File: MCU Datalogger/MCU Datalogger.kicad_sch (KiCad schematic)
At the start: 25 parts, among them U1 24LC1025, U2 DS1337S_, U3 24LC1025, U4 ATMEGA328P-AU, Y1 32.768KHz, Y2 16MHz

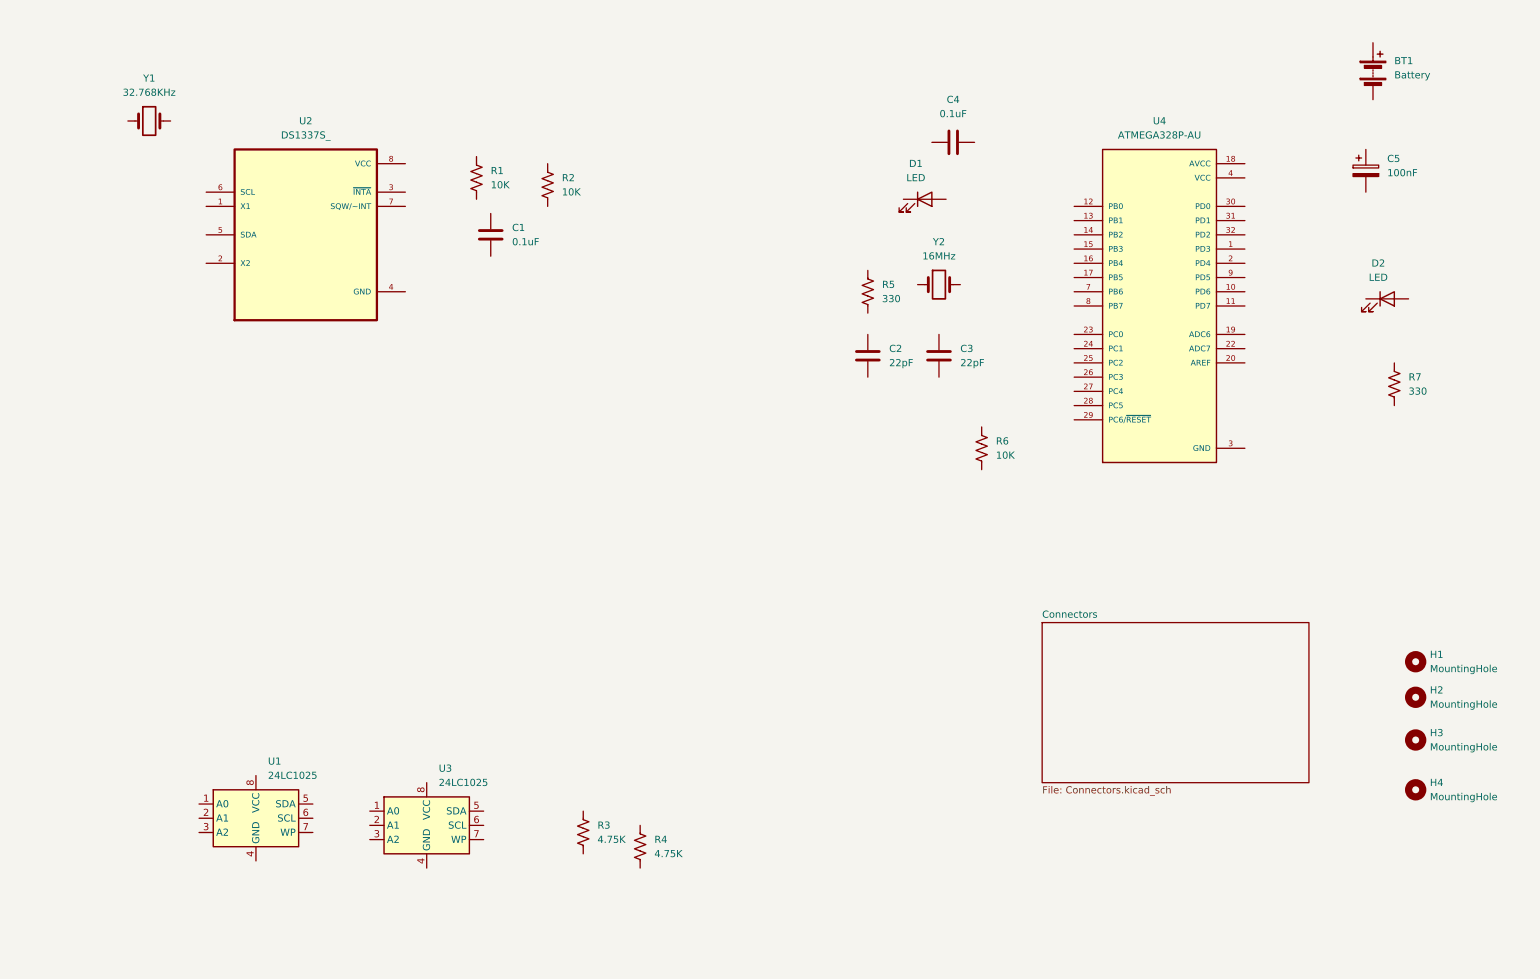
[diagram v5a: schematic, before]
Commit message: main: Wired sheet 1 with connections and nets
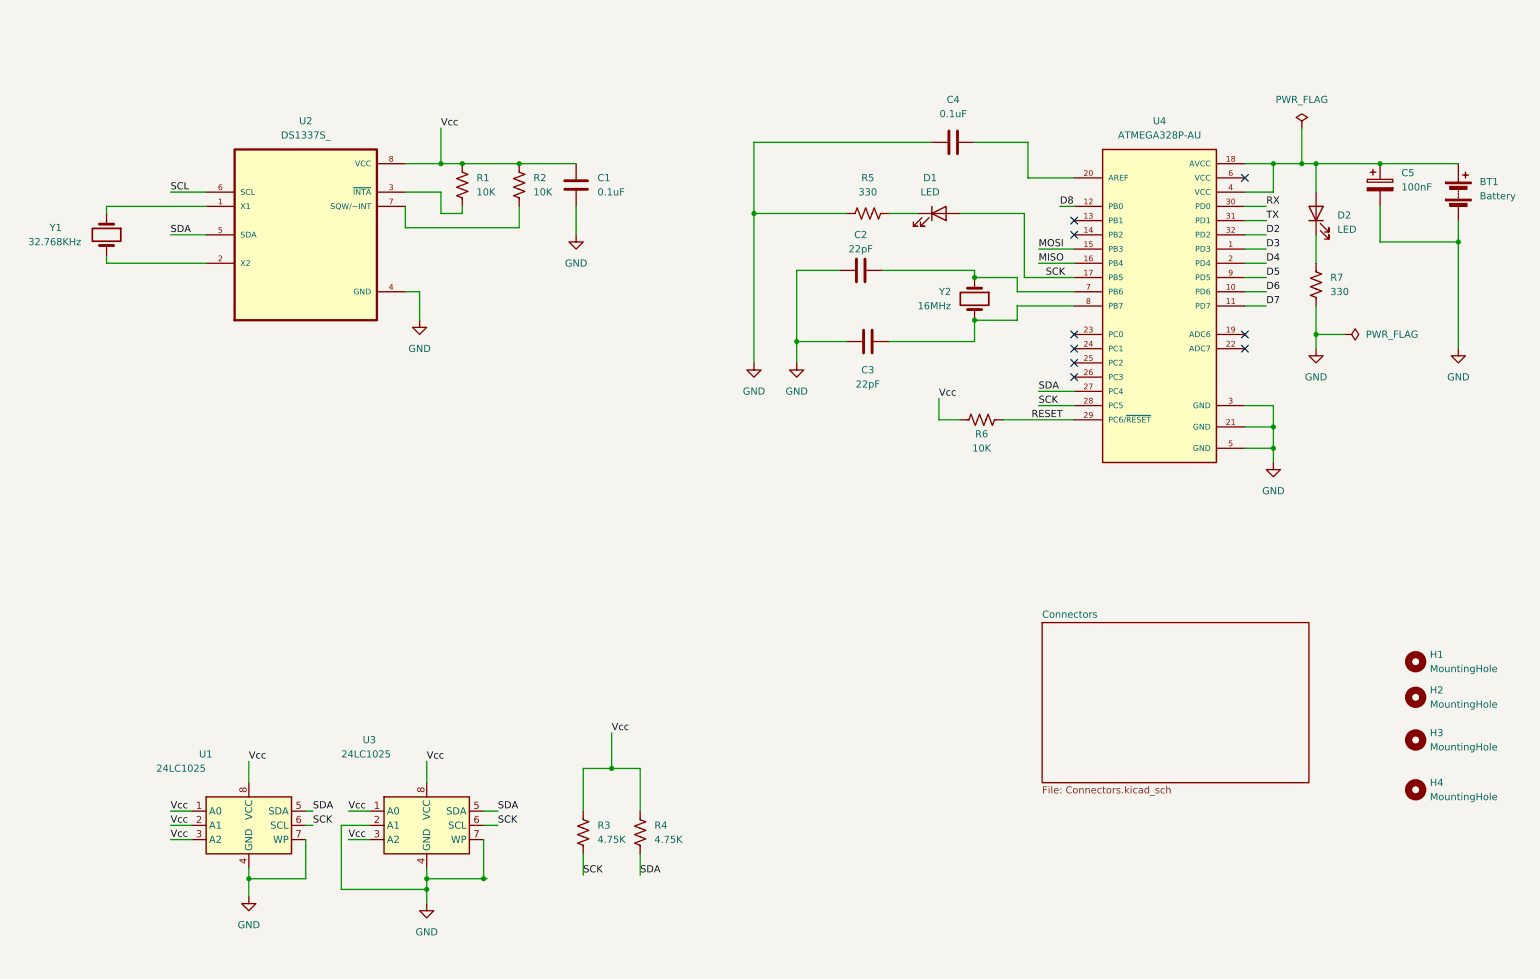
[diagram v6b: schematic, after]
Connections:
- net GND: now also BT1.2 (-), C1.2, C2.1, C3.1, C4.1, C5.2, R5.1, R7.2, U1.4 (GND), U1.7 (WP), U2.4 (GND), U3.2 (A1), U3.4 (GND), U3.7 (WP)
- net at C5.1: now also BT1.1 (+), D2.2 (A), U4.18 (AVCC), U4.4 (VCC)
- net at D1.1 (K): now also R5.2
- net SCK: now reaches D1.2 (A)
- net SCK: now also R3.2, U1.6 (SCL), U3.6 (SCL), U4.17 (PB5), U4.28 (PC5)
- net at Y1.1: now also U2.1 (X1)
- net at Y1.2: now also U2.2 (X2)
- net Vcc: now reaches C1.1
- net Vcc: now also R1.1, R2.1, R3.1, R4.1, R6.1, U1.1 (A0), U1.2 (A1), U1.3 (A2), U1.8 (VCC), U2.8 (VCC), U3.1 (A0), U3.3 (A2), U3.8 (VCC)
- net SDA: now reaches U1.5 (SDA)
- net SDA: now also R4.2, U2.5 (SDA), U3.5 (SDA), U4.27 (PC4)
- net at C4.2: now also U4.20 (AREF)
- net at R2.2: now also U2.7 (SQW/~INT)
- net at Y2.1: now also C2.2, U4.7 (PB6)
- net at Y2.2: now also C3.2, U4.8 (PB7)
- net at D2.1 (K): now also R7.1
- net at U2.3 (~{INTA}): now also R1.2
- net SCL: now reaches U2.6 (SCL)
- net D3: now reaches U4.1 (PD3)
- net D6: now reaches U4.10 (PD6)
- net D7: now reaches U4.11 (PD7)
- net D8: now reaches U4.12 (PB0)
- net MOSI: now reaches U4.15 (PB3)
- net MISO: now reaches U4.16 (PB4)
- net D4: now reaches U4.2 (PD4)
- net RESET: now reaches U4.29 (PC6/~{RESET})
- net RESET: now also R6.2
- net RX: now reaches U4.30 (PD0)
- net TX: now reaches U4.31 (PD1)
- net D2: now reaches U4.32 (PD2)
- net D5: now reaches U4.9 (PD5)
- net VCC: no longer names the net of U4.6 (VCC)
- net VCC: no longer U4.4 (VCC)
- no-connect marks 0 -> 9
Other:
- moved on the sheet: BT1, C1, C2, C3, C5, D1, D2, R1, R2, R4, R5, R6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

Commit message: New computer update with complete schematic connections
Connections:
- net SCL is gone; now on net SCK: U2.6 (SCL)
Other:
- sheet Connectors ports: added D2, D3, D4, D5, D6, D7, D8, GND, MISO, MOSI, RESET, RX, SCK, SDA, TX, Vcc; removed none

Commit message: main: Finalizing schematic
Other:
- note added: "EEPROM"
- note added: "MCU"
- note added: "Mounting"
- note added: "Real time clock"
